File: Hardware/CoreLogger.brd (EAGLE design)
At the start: 100 x 80 mm, 60 parts, among them J1 CONN_32.54_SCREW, J10 CONN_42.54_SCREW, J11 CONN_32.54_SCREW, J12 CONN_32.54_SCREW, J2 CONN_32.54_SCREW, J4 CONN_5, J6 CONN_42.54_SCREW, J7 CONN_42.54_SCREW, J8 CONN_42.54_SCREW, Q1 DMG3404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

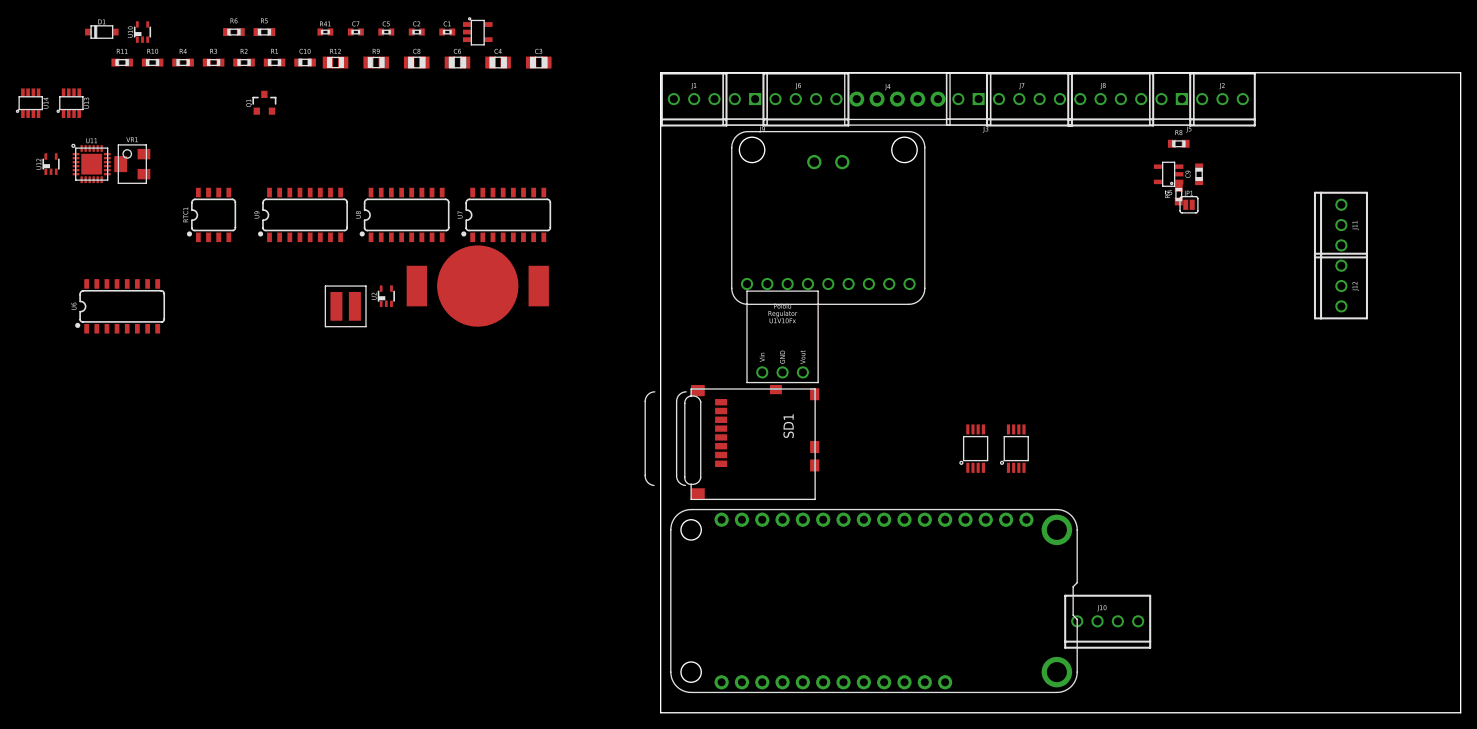
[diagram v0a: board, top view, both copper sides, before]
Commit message: Routing and minor design updates
The majority of functionality is present, passes DRC, need to add polygons and test points, along with labeling
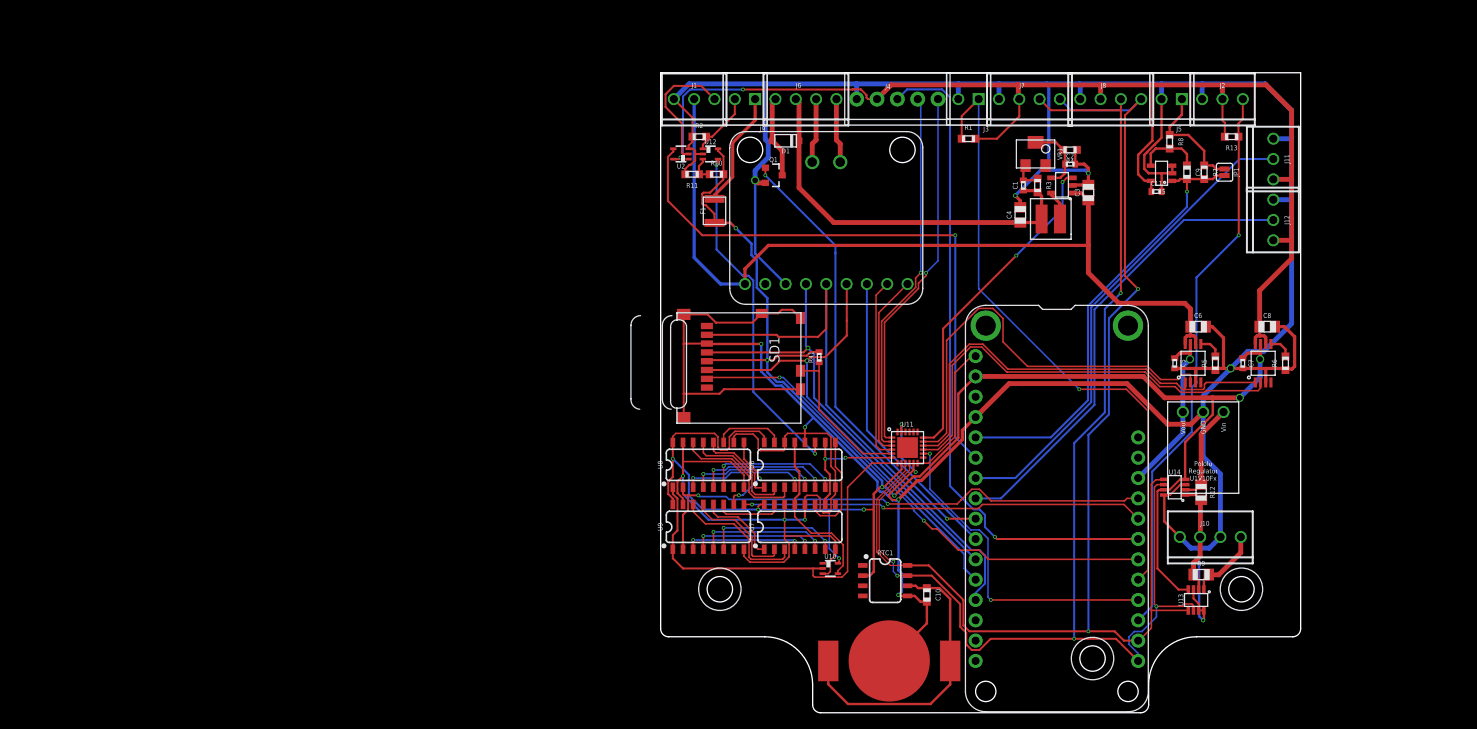
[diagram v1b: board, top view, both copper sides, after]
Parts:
- added C11: 0.1uF, bschulz_passives:C0402
- added F1: PPTC100MA1210, bschulz:1210_BOURNS
- added H1, H2, H3: (no value), bschulz:4_40
- added R13: 10k, bschulz_passives:R0603
- moved U13 153.7 mm to (66.9, 14.1), turned to 180 degrees
- moved U14 150.8 mm to (64.3, 28.2), turned to 90 degrees
- moved R6 137.8 mm to (78.1, 43.7), turned to 90 degrees
- moved R5 125.9 mm to (69.3, 43.7), turned to 90 degrees
- moved R9 121.4 mm to (67.6, 17.3)
- moved R12 120.8 mm to (67.6, 27.6), turned to 270 degrees
- moved C7 118.3 mm to (72.8, 43.7), turned to 270 degrees
- moved VR1 112.9 mm to (46.9, 69.8), turned to 270 degrees
- moved R4 111.4 mm to (51.2, 70.4), turned to 180 degrees
- moved C8 111.3 mm to (75.8, 48.3)
- moved U10 109.0 mm to (21.2, 18.0), turned to 270 degrees
- moved U11 108.0 mm to (30.9, 33.1)
- moved C5 106.9 mm to (64.3, 43.7), turned to 270 degrees
- moved R3 104.1 mm to (47.1, 65.9), turned to 270 degrees
- moved C10 102.3 mm to (33.3, 14.7), turned to 270 degrees
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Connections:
- removed net 3V3_EN: U4.1
- removed net 5V_EN: U3.1
- removed net VCC: U6.16, U7.16, U8.16, U9.16
- removed net V_CAP: R10.2
- new net 3V3_WIND: F1.2, J9.P2
- new net AUX_EN: U11.16, U3.1, U4.1
- net !RST: now also U11.6
- net 3V3: now also F1.1, R10.2, U10.5, U12.5, U6.16, U7.16, U8.16, U9.16
- net 3V3_AUX: now also C11.1, R13.2; no longer J9.P2, U10.5, U12.5
- net 3V3_FAULT: now also U11.15
- net 5V_FAULT: now also U11.17
- net GND: now also C11.2
- net HEATER_EN: now also U11.18
- net LOAD: now also U11.7
- net S0: now also U11.1
- net S1: now also U11.2
- net SAP_FAULT: now also U11.4
- net SAP_HEATER_SW: now also MS1.9
- net SAP_READY: now also U11.3
- net SD_CD: now also U11.5
- net SOIL_1: now also J12.2; no longer J11.2
- net SOIL_2: now also J11.2; no longer J12.2
- net WATER_TEMP: now also R13.1
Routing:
- net GND: track 0.00 -> 576.7 mm, vias 0 -> 14
- net 3V3: track 0.00 -> 246.0 mm, vias 0 -> 10
- net SDA: track 0.00 -> 166.8 mm, vias 0 -> 5
- net SCL: track 0.00 -> 160.4 mm, vias 0 -> 2
- net 3V3_AUX: track 0.00 -> 159.7 mm, vias 0 -> 2
- net 5V_AUX: track 0.00 -> 106.2 mm
- net F_IN: track 0.00 -> 83.2 mm, vias 0 -> 1
- net RAIN_TIP: track 0.00 -> 78.7 mm, vias 0 -> 1
- net WATER_DEPTH_3V3: track 0.00 -> 73.4 mm, vias 0 -> 1
- net WATER_TEMP: track 0.00 -> 70.6 mm, vias 0 -> 1
- net MISO: track 0.00 -> 69.8 mm
- net CLK: track 0.00 -> 66.7 mm, vias 0 -> 2
- net SD_CS: track 0.00 -> 63.6 mm, vias 0 -> 2
- net MOSI: track 0.00 -> 61.8 mm, vias 0 -> 1
- net SOIL_2: track 0.00 -> 60.7 mm
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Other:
- board size 100 x 80 mm -> 80 x 80 mm

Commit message: Further updates, ready for final review
Added silkscreen and minor layout improvements
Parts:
- added C12, C13, C14, C15, C16, C17: 0.1uF, bschulz_passives:C0402
- added H4, H5: (no value), bschulz:4_40
- moved F1 2.03 mm to (6.73, 60.7)
- moved R4 1.27 mm to (51.2, 69.1)
- moved C3 1.27 mm to (53.5, 63.8)
- moved L1 1.27 mm to (48.8, 60.5)
- moved C1 1.27 mm to (45.3, 64.6)
- moved C2 1.27 mm to (51.2, 67.3)
- moved C4 1.27 mm to (45.0, 61.0)
- moved R1 1.27 mm to (38.5, 70.5)
- moved R10 1.27 mm to (6.99, 66.0)
- moved R11 1.27 mm to (3.94, 66.0)
- moved R2 1.27 mm to (4.83, 70.7)
- moved R3 1.27 mm to (47.1, 64.6)
- moved U1 1.27 mm to (50.2, 64.6)
- moved U12 1.27 mm to (6.22, 68.6)
- moved U2 1.27 mm to (2.54, 68.6)
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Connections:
- net 3V3: now also C12.1, C13.1, C14.1, C15.1, C16.1, C17.1
- net GND: now also C12.2, C13.2, C14.2, C15.2, C16.2, C17.2
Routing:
- net GND: track 576.7 -> 590.9 mm
- net 3V3: track 246.0 -> 254.5 mm
- net 5V_AUX: track 106.2 -> 102.7 mm
- net 3V3_AUX: track 159.7 -> 162.1 mm
- net 3V3_WIND: track 14.6 -> 16.6 mm
- net WIND_PULSE: track 8.31 -> 9.88 mm
- net WATER_DEPTH: track 16.3 -> 17.6 mm
- net RAIN_TIP: track 78.7 -> 79.9 mm
- net PULSE_DIG: track 43.8 -> 42.5 mm
- net WATER_DEPTH_3V3: track 73.4 -> 72.1 mm
- net SAP_HEATER+: track 49.0 -> 49.5 mm
- net HEATER_EN: track 41.4 -> 40.9 mm
- added copper zone on layer 1, net 3V3_AUX
- added copper zone on layer 1, net 5V_AUX
- added copper zone on layer 1, net GND
- added copper zone on layer 16, net GND
- added copper zone on layer 1, net N$3
- added copper zone on layer 1, net N$6
- added copper zone on layer 1, net SAP_HEATER+
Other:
- board text added: "3v3"
- board text added: "5v"
- board text added: "Fin"
- board text added: "GND"
- board text added: "H+"
- board text added: "H-"
- board text added: "Pyro"
- board text added: "S0"
- board text added: "S1"
- board text added: "SCL"
- board text added: "SDA"
- board text added: "Soil1"
- board text added: "Soil2"
- board text added: "T+"
- board text added: "T-"
- board text added: "Tip"
- board text added: "WD"
- board text added: "WT"
- board text added: "Wind"
